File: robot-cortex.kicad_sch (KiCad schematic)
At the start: 45 parts, among them IC1 THVD2410VDRCR, J1 USB4110GFA, M1 THRU_HOLE_PAD, M2 THRU_HOLE_PAD, U1 C2901617, U2 STM32G431CBT6, U3 TLE9250XSJXUMA1, U4 DF52-3S-0.8H(21), U5 DF52-4S-0.8H(21), U6 SPX3819M5-L-5-0

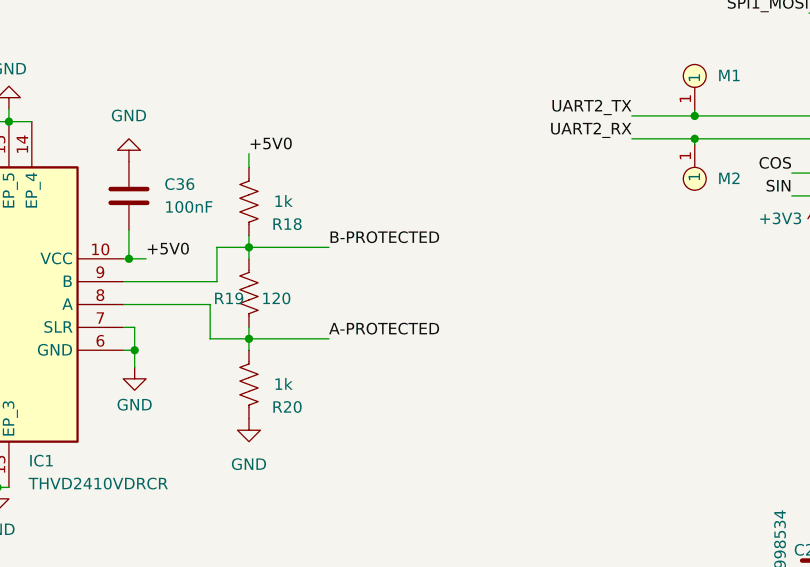
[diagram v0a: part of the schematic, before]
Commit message: routed but want to reroute differential pairs
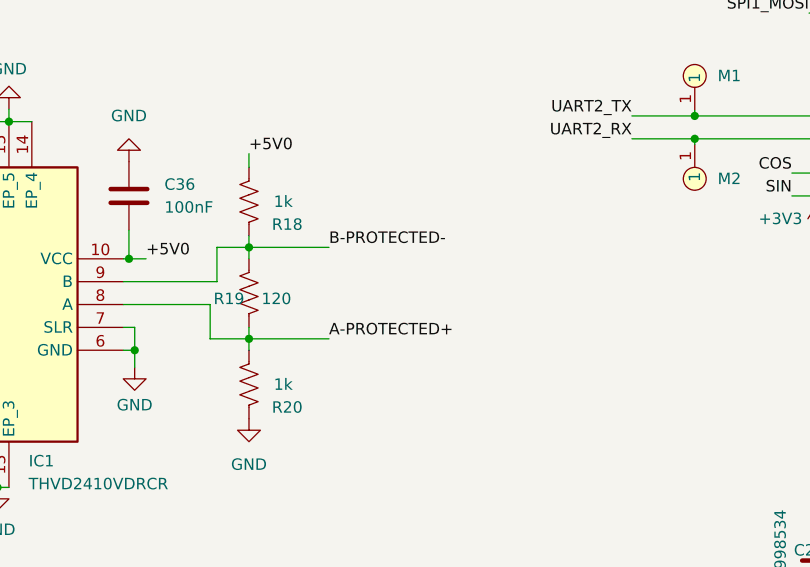
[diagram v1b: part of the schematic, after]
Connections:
- net A-PROTECTED: no longer IC1.8 (A), R19.1, R20.2
- net B-PROTECTED: no longer IC1.9 (B), R18.1, R19.2
- new net A-PROTECTED+: IC1.8 (A), R19.1, R20.2
- new net B-PROTECTED-: IC1.9 (B), R18.1, R19.2
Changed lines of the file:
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@@
     (effects (font (size 1.27 1.27)) (justify right bottom))
   )
-  (label "B-PROTECTED" (at 104.14 132.08 0) (fields_autoplaced)
+  (label "B-PROTECTED-" (at 104.14 132.08 0) (fields_autoplaced)
     (effects (font (size 1.27 1.27)) (justify left bottom))
   )
-  (label "A-PROTECTED" (at 104.14 142.24 0) (fields_autoplaced)
+  (label "A-PROTECTED+" (at 104.14 142.24 0) (fields_autoplaced)
     (effects (font (size 1.27 1.27)) (justify left bottom))
   )

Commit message: rerouted
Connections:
- net B-PROTECTED is gone; now on net C-: U3.6 (CANL), U5.2
- net B-PROTECTED- is gone; now on net C+: IC1.9 (B), R18.1, R19.2
- net A-PROTECTED renamed C+
- net A-PROTECTED+ renamed C-
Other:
- moved on the sheet: U5
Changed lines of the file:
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@@
   (junction (at 160.655 130.175) (diameter 0) (color 0 0 0 0)
   )
-  (junction (at 261.62 34.925) (diameter 0) (color 0 0 0 0)
-  )
   (junction (at 103.505 195.58) (diameter 0) (color 0 0 0 0)
   )
@@
   (junction (at 238.76 215.9) (diameter 0) (color 0 0 0 0)
   )
-  (junction (at 278.765 40.005) (diameter 0) (color 0 0 0 0)
+  (junction (at 278.13 38.1) (diameter 0) (color 0 0 0 0)
   )
   (junction (at 163.83 264.795) (diameter 0) (color 0 0 0 0)
@@
   (junction (at 275.59 254) (diameter 0) (color 0 0 0 0)
   )
-  (junction (at 261.62 32.385) (diameter 0) (color 0 0 0 0)
-  )
   (junction (at 128.27 248.285) (diameter 0) (color 0 0 0 0)
   )
@@
     (stroke (width 0) (type default))
   )
-  (wire (pts (xy 260.985 34.925) (xy 261.62 34.925))
-    (stroke (width 0) (type default))
-  )
   (wire (pts (xy 116.205 273.685) (xy 109.855 273.685))
     (stroke (width 0) (type default))
@@
     (stroke (width 0) (type default))
   )
+  (wire (pts (xy 260.35 30.48) (xy 266.7 30.48))
+    (stroke (width 0) (type default))
+  )
   (wire (pts (xy 249.555 235.585) (xy 251.46 235.585))
     (stroke (width 0) (type default))
@@
     (stroke (width 0) (type default))
   )
-  (wire (pts (xy 261.62 32.385) (xy 267.335 32.385))
-    (stroke (width 0) (type default))
-  )
   (wire (pts (xy 121.285 274.955) (xy 121.285 273.685))
     (stroke (width 0) (type default))
@@
     (stroke (width 0) (type default))
   )
-  (wire (pts (xy 256.54 27.94) (xy 261.62 27.94))
-    (stroke (width 0) (type default))
-  )
-  (wire (pts (xy 278.765 27.305) (xy 278.765 40.005))
+  (wire (pts (xy 278.13 25.4) (xy 278.13 38.1))
     (stroke (width 0) (type default))
   )
@@
     (stroke (width 0) (type default))
   )
-  (wire (pts (xy 260.985 32.385) (xy 261.62 32.385))
-    (stroke (width 0) (type default))
-  )
   (wire (pts (xy 267.335 278.765) (xy 272.415 278.765))
     (stroke (width 0) (type default))
   )
-  (wire (pts (xy 256.54 38.1) (xy 261.62 38.1))
-    (stroke (width 0) (type default))
-  )
   (wire (pts (xy 161.29 171.45) (xy 158.75 171.45))
     (stroke (width 0) (type default))
@@
     (stroke (width 0) (type default))
   )
-  (wire (pts (xy 261.62 34.925) (xy 267.335 34.925))
-    (stroke (width 0) (type default))
-  )
   (wire (pts (xy 271.78 164.465) (xy 273.685 164.465))
     (stroke (width 0) (type default))
@@
     (stroke (width 0) (type default))
   )
-  (wire (pts (xy 278.765 40.005) (xy 278.765 41.91))
+  (wire (pts (xy 278.13 38.1) (xy 278.13 40.005))
     (stroke (width 0) (type default))
   )
-  (wire (pts (xy 267.335 23.495) (xy 267.335 29.845))
+  (wire (pts (xy 266.7 21.59) (xy 266.7 27.94))
     (stroke (width 0) (type default))
   )
@@
     (stroke (width 0) (type default))
   )
-  (wire (pts (xy 261.62 27.94) (xy 261.62 32.385))
-    (stroke (width 0) (type default))
-  )
   (wire (pts (xy 269.875 154.94) (xy 273.685 154.94))
     (stroke (width 0) (type default))
@@
     (stroke (width 0) (type default))
   )
-  (wire (pts (xy 261.62 38.1) (xy 261.62 34.925))
-    (stroke (width 0) (type default))
-  )
   (wire (pts (xy 208.915 94.615) (xy 206.375 94.615))
     (stroke (width 0) (type default))
@@
     (stroke (width 0) (type default))
   )
+  (wire (pts (xy 260.35 33.02) (xy 266.7 33.02))
+    (stroke (width 0) (type default))
+  )
   (wire (pts (xy 272.415 241.3) (xy 272.415 240.665))
     (stroke (width 0) (type default))
@@
     (effects (font (size 1.27 1.27)) (justify right bottom))
   )
-  (label "B-PROTECTED" (at 256.54 27.94 180) (fields_autoplaced)
-    (effects (font (size 1.27 1.27)) (justify right bottom))
-  )
-  (label "B-PROTECTED-" (at 104.14 132.08 0) (fields_autoplaced)
-    (effects (font (size 1.27 1.27)) (justify left bottom))
-  )
-  (label "A-PROTECTED+" (at 104.14 142.24 0) (fields_autoplaced)
-    (effects (font (size 1.27 1.27)) (justify left bottom))
-  )
   (label "ISENSE_C" (at 210.185 125.095 0) (fields_autoplaced)
     (effects (font (size 1.27 1.27)) (justify left bottom))
@@
     (effects (font (size 1.27 1.27)) (justify left bottom))
   )
-  (label "CANH" (at 203.2 30.48 0) (fields_autoplaced)
+  (label "C+" (at 203.2 30.48 0) (fields_autoplaced)
     (effects (font (size 1.27 1.27)) (justify left bottom))
   )
@@
     (effects (font (size 1.27 1.27)) (justify left bottom))
   )
-  (label "CANH" (at 260.985 34.925 180) (fields_autoplaced)
+  (label "C+" (at 260.35 33.02 180) (fields_autoplaced)
     (effects (font (size 1.27 1.27)) (justify right bottom))
   )
@@
     (effects (font (size 1.27 1.27)) (justify left bottom))
   )
-  (label "VBAT" (at 267.335 23.495 180) (fields_autoplaced)
+  (label "VBAT" (at 266.7 21.59 180) (fields_autoplaced)
     (effects (font (size 1.27 1.27)) (justify right bottom))
   )
@@
     (effects (font (size 1.27 1.27)) (justify right bottom))
   )
+  (label "C-" (at 104.14 142.24 0) (fields_autoplaced)
+    (effects (font (size 1.27 1.27)) (justify left bottom))
+  )
   (label "SPI1_SCK" (at 157.48 100.965 180) (fields_autoplaced)
     (effects (font (size 1.27 1.27)) (justify right bottom))
   )
-  (label "CANL" (at 260.985 32.385 180) (fields_autoplaced)
+  (label "C-" (at 260.35 30.48 180) (fields_autoplaced)
     (effects (font (size 1.27 1.27)) (justify right bottom))
   )
@@
     (effects (font (size 1.27 1.27)) (justify right bottom))
   )
+  (label "C+" (at 104.14 132.08 0) (fields_autoplaced)
+    (effects (font (size 1.27 1.27)) (justify left bottom))
+  )
   (label "SWCLK" (at 208.915 60.325 0) (fields_autoplaced)
     (effects (font (size 1.27 1.27)) (justify left bottom))
@@
     (effects (font (size 1.27 1.27)) (justify right bottom))
   )
-  (label "CANL" (at 203.2 33.02 0) (fields_autoplaced)
+  (label "C-" (at 203.2 33.02 0) (fields_autoplaced)
     (effects (font (size 1.27 1.27)) (justify left bottom))
   )
@@
     (effects (font (size 1.27 1.27)) (justify left bottom))
   )
-  (label "A-PROTECTED" (at 256.54 38.1 180) (fields_autoplaced)
-    (effects (font (size 1.27 1.27)) (justify right bottom))
-  )
   (symbol (lib_id "power:+3V3") (at 158.115 130.175 0) (unit 1)
     (in_bom yes) (on_board yes) (dnp no)
@@
     )
   )
-  (symbol (lib_id "foc-pcb:DF52-4S-0.8H(21)") (at 273.685 33.655 0) (unit 1)
+  (symbol (lib_id "foc-pcb:DF52-4S-0.8H(21)") (at 273.05 31.75 0) (unit 1)
     (in_bom yes) (on_board yes) (dnp no)
-    (property "Reference" "U5" (at 273.05 22.225 0)
+    (property "Reference" "U5" (at 272.415 20.32 0)
       (effects (font (size 1.27 1.27)))
     )
-    (property "Value" "DF52-4S-0.8H(21)" (at 280.035 24.765 0)
+    (property "Value" "DF52-4S-0.8H(21)" (at 279.4 22.86 0)
       (effects (font (size 1.27 1.27)))
     )
-    (property "Footprint" "robot-cortex:DF52-4S-0.8H(21)" (at 276.225 47.625 0)
+    (property "Footprint" "robot-cortex:DF52-4S-0.8H(21)" (at 275.59 45.72 0)
       (effects (font (size 1.27 1.27)) hide)
     )
-    (property "Datasheet" "" (at 276.225 36.195 0)
+    (property "Datasheet" "" (at 275.59 34.29 0)
       (effects (font (size 1.27 1.27)) hide)
     )
@@
     )
   )
-  (symbol (lib_id "power:GND") (at 278.765 41.91 0) (mirror y) (unit 1)
+  (symbol (lib_id "power:GND") (at 278.13 40.005 0) (mirror y) (unit 1)
     (in_bom yes) (on_board yes) (dnp no)
-    (property "Reference" "#PWR026" (at 278.765 48.26 0)
+    (property "Reference" "#PWR026" (at 278.13 46.355 0)
       (effects (font (size 1.27 1.27)) hide)
     )
-    (property "Value" "GND" (at 275.59 43.815 0)
+    (property "Value" "GND" (at 274.955 41.91 0)
       (effects (font (size 1.27 1.27)))
     )
-    (property "Footprint" "" (at 278.765 41.91 0)
+    (property "Footprint" "" (at 278.13 40.005 0)
       (effects (font (size 1.27 1.27)) hide)
     )
-    (property "Datasheet" "" (at 278.765 41.91 0)
+    (property "Datasheet" "" (at 278.13 40.005 0)
       (effects (font (size 1.27 1.27)) hide)
     )
@@
     )
   )
-  (symbol (lib_id "power:GND") (at 267.335 37.465 0) (mirror y) (unit 1)
+  (symbol (lib_id "power:GND") (at 266.7 35.56 0) (mirror y) (unit 1)
     (in_bom yes) (on_board yes) (dnp no)
-    (property "Reference" "#PWR024" (at 267.335 43.815 0)
+    (property "Reference" "#PWR024" (at 266.7 41.91 0)
       (effects (font (size 1.27 1.27)) hide)
     )
-    (property "Value" "GND" (at 264.16 39.37 0)
+    (property "Value" "GND" (at 263.525 37.465 0)
       (effects (font (size 1.27 1.27)))
     )
-    (property "Footprint" "" (at 267.335 37.465 0)
+    (property "Footprint" "" (at 266.7 35.56 0)
       (effects (font (size 1.27 1.27)) hide)
     )
-    (property "Datasheet" "" (at 267.335 37.465 0)
+    (property "Datasheet" "" (at 266.7 35.56 0)
       (effects (font (size 1.27 1.27)) hide)
     )

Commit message: more routing tweaks
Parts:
- U3: now not fitted; now left out of the parts list
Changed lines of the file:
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@@
   )
   (symbol (lib_id "foc-pcb:TLE9250XSJXUMA1") (at 192.405 31.75 0) (unit 1)
-    (in_bom yes) (on_board yes) (dnp no)
+    (in_bom no) (on_board yes) (dnp yes)
     (property "Reference" "U3" (at 187.96 21.59 0)
       (effects (font (size 1.27 1.27)))

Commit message: blah
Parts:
- removed C10, C3, C6, C8: 100nF, robot-cortex:C_0402_1005Metric, symbol foc-pcb:Capacitor
- removed C2, C5, C7, C9: C2998534, robot-cortex:C_0603_1608Metric, symbol foc-pcb:Capacitor
- removed D4: C84264, robot-cortex:LED_0603_1608Metric, symbol foc-pcb:LED
- removed M1, M2: THRU_HOLE_PAD, robot-cortex:TEARDROP, symbol foc-pcb:THRU_HOLE_PAD
- removed R2: 4.7k, robot-cortex:R_0402_1005Metric, symbol foc-pcb:Resistor
- removed R3: 470, robot-cortex:R_0402_1005Metric, symbol foc-pcb:Resistor
- removed U1: C2901617, robot-cortex:ECS-1633-480-BN-TR, symbol foc-pcb:OSCILLATOR-4PIN
- removed U2: STM32G431CBT6, robot-cortex:LQFP48-STM32, symbol foc-pcb:STM32G431CBtx
- removed U3: TLE9250XSJXUMA1, robot-cortex:SOIC8-TLE5009, symbol foc-pcb:TLE9250XSJXUMA1
- removed U4: DF52-3S-0.8H(21), robot-cortex:DF52-3S-0.8H(21), symbol foc-pcb:DF52-3S-0.8H(21)
- removed U6: SPX3819M5-L-5-0, robot-cortex:SOT-23-5, symbol foc-pcb:SPX3819M5-L-5-0
- added U1: DF52-4S-0.8H(21), robot-cortex:DF52-4S-0.8H(21), symbol foc-pcb:DF52-4S-0.8H(21)
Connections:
- net UART1_RX is gone; now on net UART2_RX: IC1.2 (R)
- net UART1_TX is gone; now on net UART2_TX: IC1.5 (D)
- net C+: now also U1.3
- net C-: now also U1.2
- net GND: now also U1.4, U1.5 (MNT), U1.6 (MNT)
- net VBAT: now also U1.1
- net UART1_DE renamed UART2_DE
- no-connect marks 13 -> 2
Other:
- moved on the sheet: C1, C36, IC1, R18, R19, R20
